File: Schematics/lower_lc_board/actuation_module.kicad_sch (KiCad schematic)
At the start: 13 parts, among them Q5 2N7002, U12 DMP4065S-7

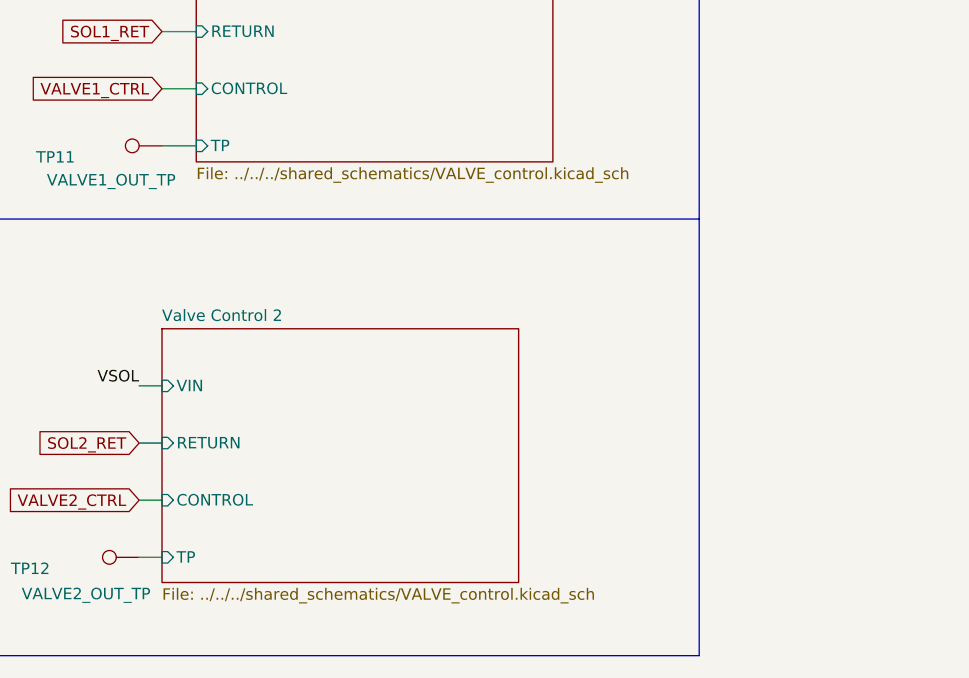
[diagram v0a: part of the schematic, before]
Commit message: organize working copy of lower valve board for merge to main
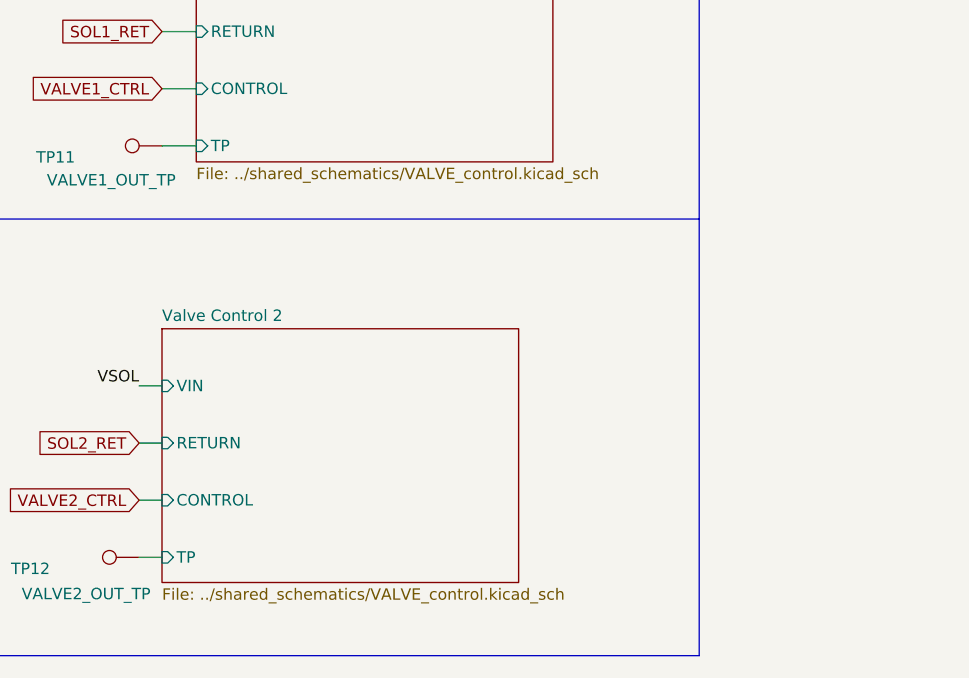
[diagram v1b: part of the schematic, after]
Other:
- sheet Valve Control 1: file ../../../shared_schematics/VALVE_control.kicad_sch -> ../shared_schematics/VALVE_control.kicad_sch
- sheet Valve Control 2: file ../../../shared_schematics/VALVE_control.kicad_sch -> ../shared_schematics/VALVE_control.kicad_sch
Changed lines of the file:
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@@
 	(label "VSOL"
 		(at 157.48 107.95 180)
-		(fields_autoplaced yes)
 		(effects
 			(font
@@
 	(label "VSOL"
 		(at 123.19 129.54 0)
-		(fields_autoplaced yes)
 		(effects
 			(font
@@
 	(label "VSOL"
 		(at 106.68 60.96 0)
-		(fields_autoplaced yes)
 		(effects
 			(font
@@
 	(label "VSOL"
 		(at 106.68 76.2 0)
-		(fields_autoplaced yes)
 		(effects
 			(font
@@
 	(label "VSOL"
 		(at 229.87 52.07 0)
-		(fields_autoplaced yes)
 		(effects
 			(font
@@
 	(label "VSOL"
 		(at 161.29 62.23 180)
-		(fields_autoplaced yes)
 		(effects
 			(font
@@
 		)
 		(instances
-			(project ""
+			(project "lower_lc_board"
 				(path "/d63798c4-e363-437e-9012-e4aff32e6642/762489dd-fdf2-4f5c-8c0c-d0a6195d3f58"
 					(reference "C46")
@@
 			)
 		)
-		(property "Datasheet" "${KIPRJMOD}/../../Documentation/pmosfet_DMP4065S-7_DS.pdf"
+		(property "Datasheet" "${KIPRJMOD}/../../Datasheets/pmosfet_DMP4065S-7_DS.pdf"
 			(at 82.55 125.73 0)
 			(effects
@@
 			)
 		)
-		(property "Datasheet" "${KIPRJMOD}/../../Documentation/nmosfet_2N7002_DS.PDF"
+		(property "Datasheet" "${KIPRJMOD}/../../Datasheets/nmosfet_2N7002_DS.PDF"
 			(at 80.01 100.33 0)
 			(effects
@@
 		)
 		(instances
-			(project ""
+			(project "lower_lc_board"
 				(path "/d63798c4-e363-437e-9012-e4aff32e6642/762489dd-fdf2-4f5c-8c0c-d0a6195d3f58"
 					(reference "#PWR075")
@@
 			)
 		)
-		(property "Sheetfile" "../../../shared_schematics/VALVE_control.kicad_sch"
+		(property "Sheetfile" "../shared_schematics/VALVE_control.kicad_sch"
 			(at 163.83 83.6426 0)
 			(effects
@@
 			)
 		)
-		(property "Sheetfile" "../../../shared_schematics/VALVE_control.kicad_sch"
+		(property "Sheetfile" "../shared_schematics/VALVE_control.kicad_sch"
 			(at 160.02 130.3786 0)
 			(effects

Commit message: update backplane orientation
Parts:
- Q5: LCSC (none) -> C8545
- U12: Digikey C182476 -> (none); JLCPCB (none) -> C182476; LCSC (none) -> C182476
